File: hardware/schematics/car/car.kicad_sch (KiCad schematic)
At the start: 14 parts, among them M1 Motor_Servo, M2 Motor_DC, Q1 Q_PMOS_Depletion, SW1 RotaryEncoder, U1 VL53L0CXV0DH1, U2 VL53L0CXV0DH1, U3 VL53L0CXV0DH1, U5 TXS0108EPW, U6 TB6612FNG

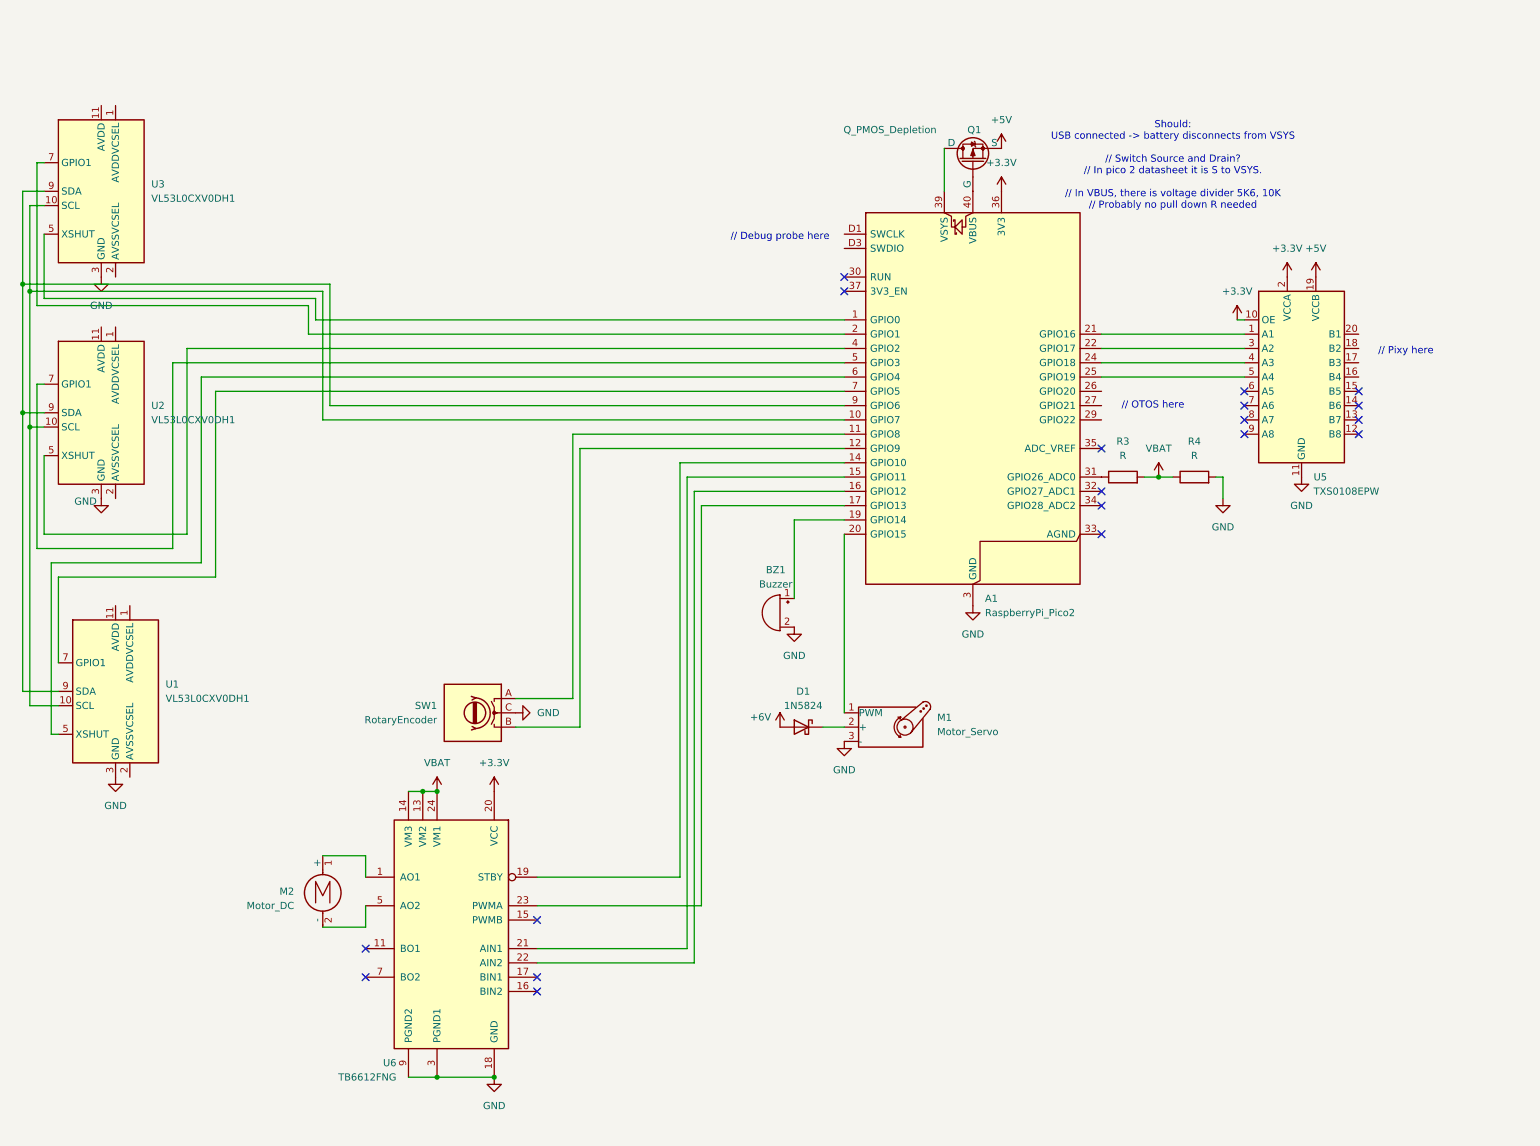
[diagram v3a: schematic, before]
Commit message: [Schematic] Add OTOS, Pixy, Debug probe, 2 buttons, fix voltage divider
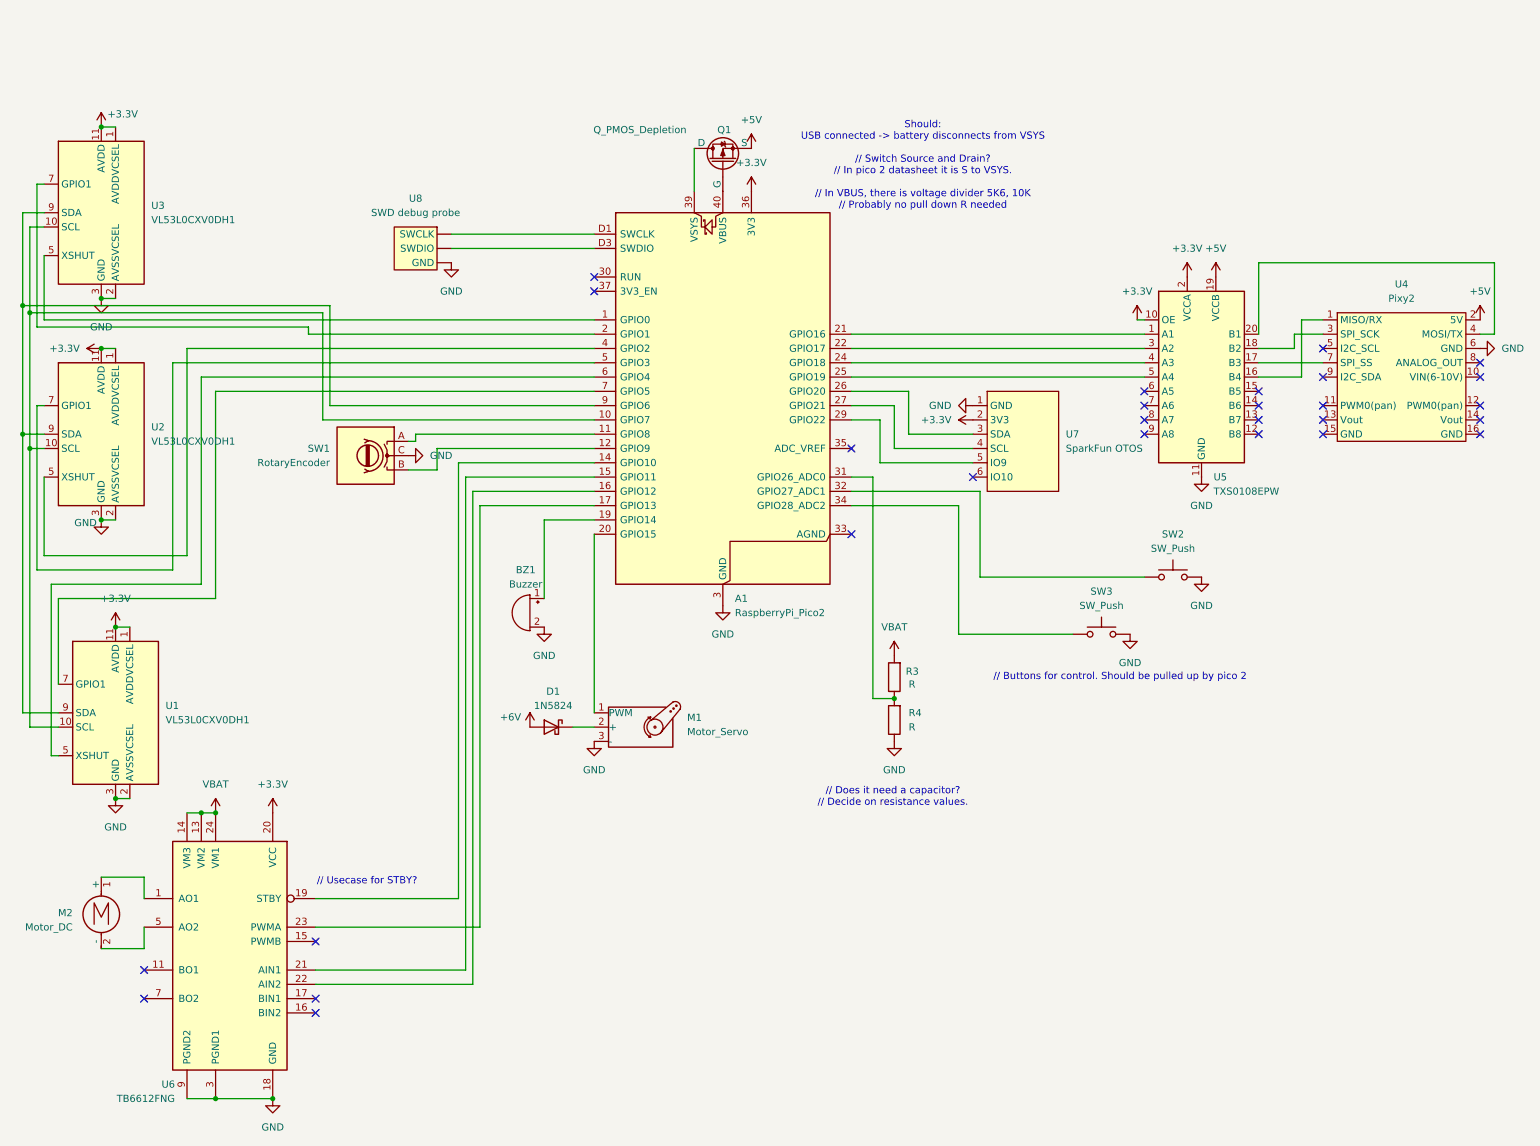
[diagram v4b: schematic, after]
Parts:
- added SW2, SW3: SW_Push, symbol Switch:SW_Push
- added U4: Pixy2, symbol xlnc_apex:Pixy2
- added U7: SparkFun OTOS, symbol xlnc_apex:SparkFun_OTOS
- added U8: SWD debug probe, symbol xlnc_apex:SWD_Debug_Probe
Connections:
- net +3.3V: now also U1.1 (AVDDVCSEL), U1.11 (AVDD), U2.1 (AVDDVCSEL), U2.11 (AVDD), U3.1 (AVDDVCSEL), U3.11 (AVDD), U7.2 (3V3)
- net +5V: now also U4.2 (5V)
- net GND: now also R4.1, U1.2 (AVSSVCSEL), U2.2 (AVSSVCSEL), U3.2 (AVSSVCSEL), SW2.2, SW3.2, U4.6 (GND), U7.1 (GND), U8. (GND); no longer R4.2
- net VBAT: no longer R4.1
- net at U5.16 (B4): now also U4.1 (MISO/RX)
- net at U5.17 (B3): now also U4.7 (SPI_SS)
- net at U5.18 (B2): now also U4.3 (SPI_SCK)
- net at U5.20 (B1): now also U4.4 (MOSI/TX)
- net at A1.31 (GPIO26_ADC0), R3.1: now also R4.2
- net at A1.26 (GPIO20): now also U7.3 (SDA)
- net at A1.27 (GPIO21): now also U7.4 (SCL)
- net at A1.29 (GPIO22): now also U7.5 (IO9)
- net at A1.32 (GPIO27_ADC1): now also SW2.1
- net at A1.34 (GPIO28_ADC2): now also SW3.1
- net at A1.D1 (SWCLK): now also U8. (GND)
- net at A1.D3 (SWDIO): now also U8. (GND)
- no-connect marks 19 -> 28
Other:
- note added: "// Buttons for control. Should be pulled up by pico 2"
- note added: "// Does it need a capacitor? // Decide on resistance values."
- note added: "// Usecase for STBY?"
- note removed: "// Debug probe here"
- note removed: "// OTOS here"
- note removed: "// Pixy here"
- moved on the sheet: A1, BZ1, D1, M1, M2, Q1, R3, R4, SW1, U1, U2, U3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

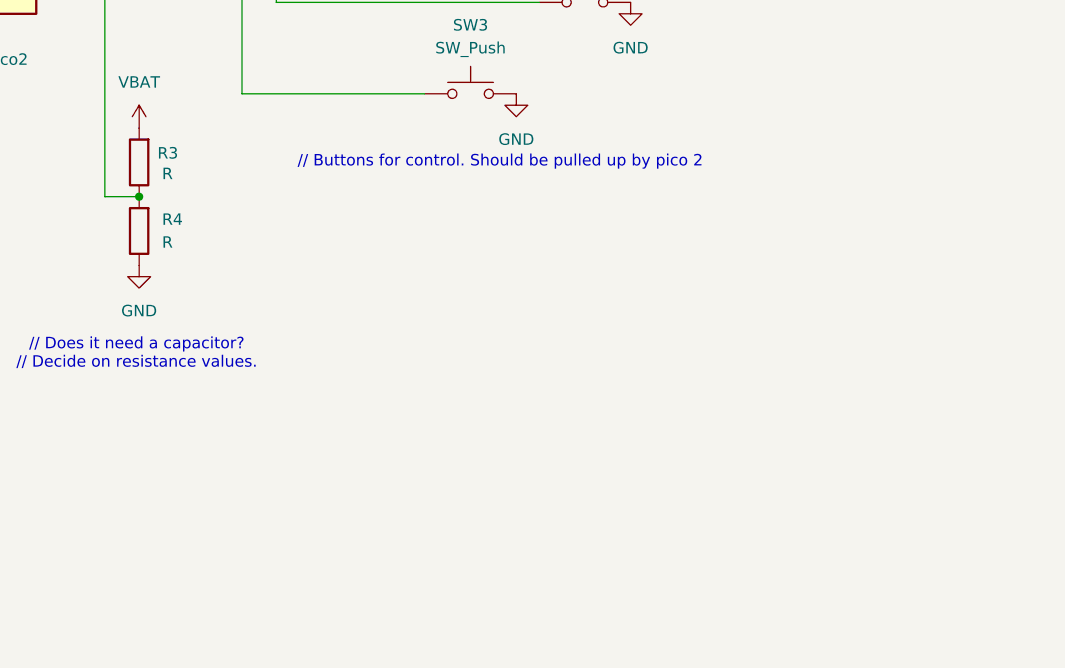
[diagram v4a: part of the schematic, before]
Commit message: [Schematic] Add buck converters, put resitances on ADC.
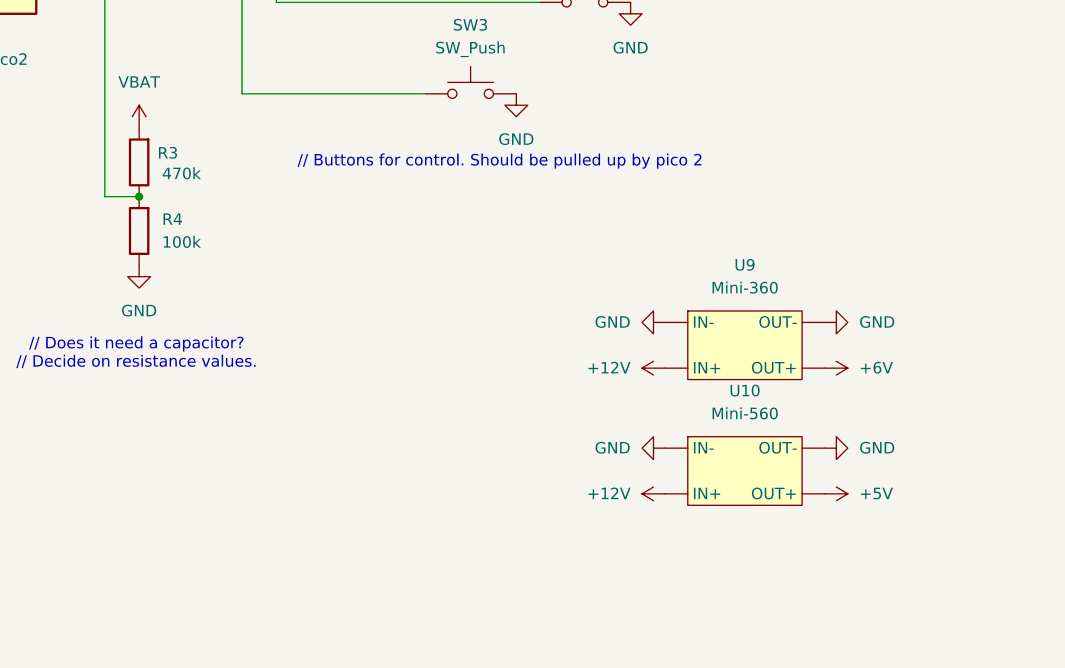
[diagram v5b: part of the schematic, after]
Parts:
- added U10: Mini-560, xlnc-foot:Buck_Mini-560, symbol xlnc_apex:mini560
- added U9: Mini-360, xlnc-foot:Buck_Mini-360, symbol xlnc_apex:mini360
- R3: value R -> 470k
- R4: value R -> 100k
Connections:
- net +5V: now also U10. (OUT+)
- net +6V: now also U9. (OUT+)
- net GND: now also U10. (OUT+), U9. (OUT+)
- new net +12V: U10. (OUT+), U9. (OUT+)

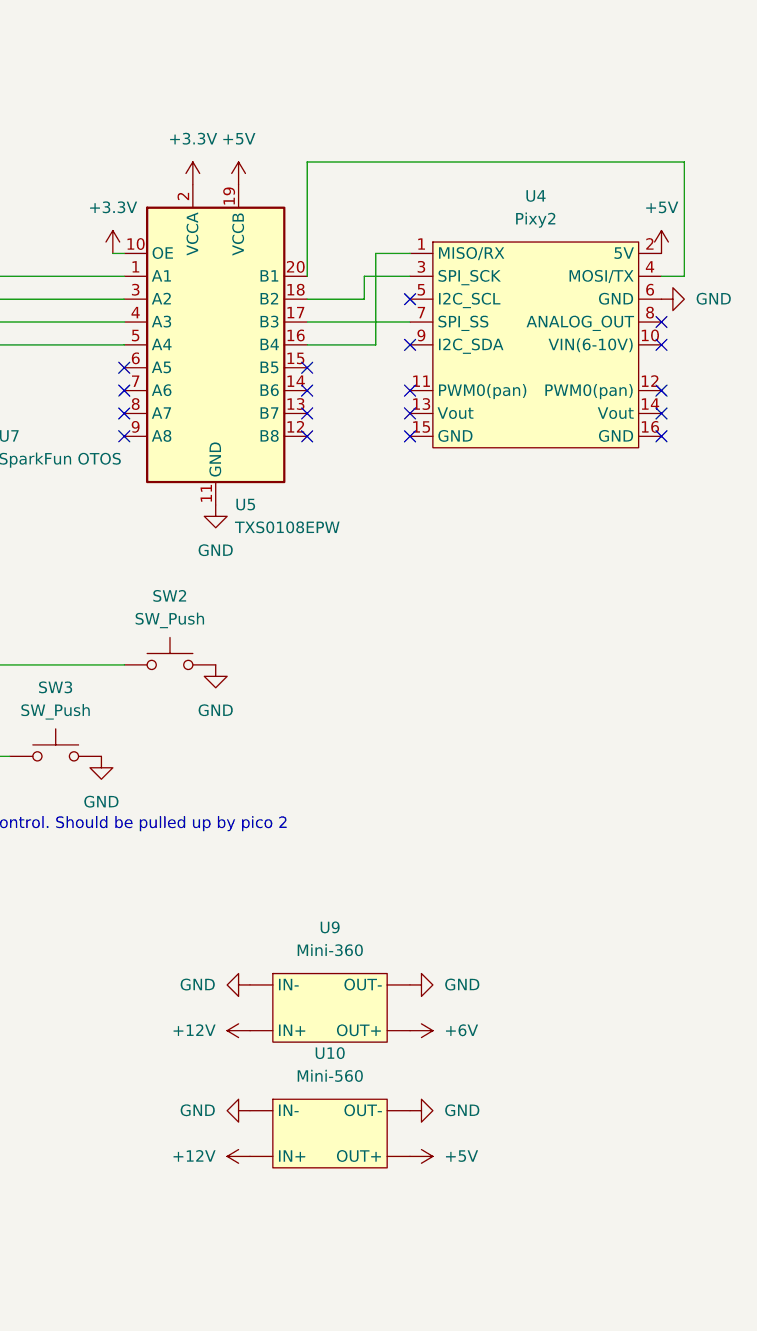
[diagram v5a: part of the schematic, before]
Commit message: [Schematic] Major work: add many perfboard footprints, fix spi wrong
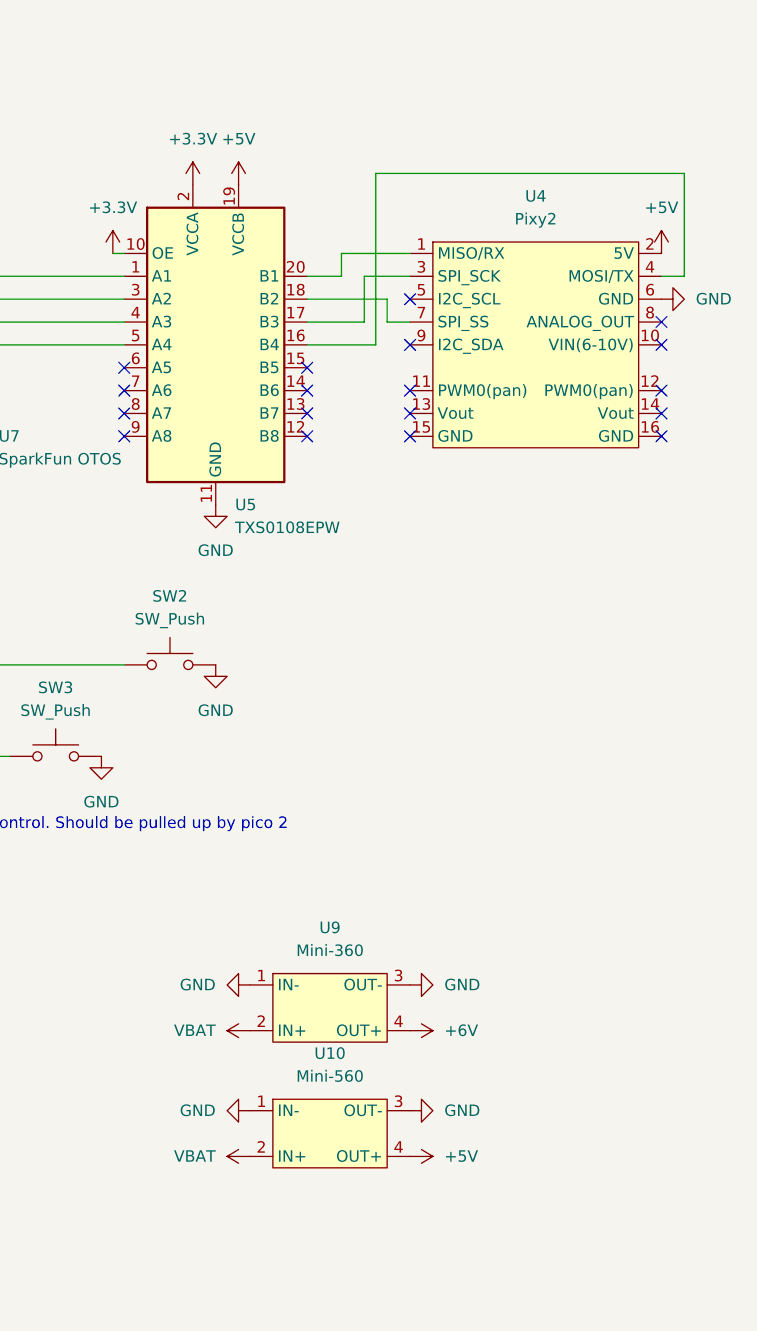
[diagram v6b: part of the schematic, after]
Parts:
- Q1: footprint (none) -> Connector_PinHeader_2.54mm:PinHeader_1x03_P2.54mm_Vertical
- R3, R4: footprint (none) -> Resistor_THT:R_Axial_DIN0204_L3.6mm_D1.6mm_P2.54mm_Vertical
- SW1, SW2, SW3: footprint (none) -> Connector_PinHeader_2.54mm:PinHeader_1x02_P2.54mm_Vertical
- U1, U2, U3: footprint Sensor_Distance:ST_VL53L1x -> xlnc-foot:VL53L0/1XV2_PinHeader_1x06_P2.54mm_Vertical
- U10: footprint xlnc-foot:Buck_Mini-560 -> xlnc-foot:Buck_Mini-560_2.54mm
- U4: footprint (none) -> xlnc-foot:Pixy2_PinHeader_1x06_P2.54mm_Vertical
- U7: footprint (none) -> Connector_PinHeader_2.54mm:PinHeader_1x05_P2.54mm_Vertical
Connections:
- net +5V: now also U10.4 (OUT+); no longer U10. (OUT+)
- net +6V: now also U9.4 (OUT+); no longer U9. (OUT+)
- net GND: now also U10.1 (IN-), U10.3 (OUT-), U9.1 (IN-), U9.3 (OUT-); no longer U10. (OUT+), U9. (OUT+)
- net VBAT: now also U10.2 (IN+), U9.2 (IN+)
- net at U5.16 (B4): now also U4.4 (MOSI/TX); no longer U4.1 (MISO/RX)
- net at U5.17 (B3): now also U4.3 (SPI_SCK); no longer U4.7 (SPI_SS)
- net at U5.18 (B2): now also U4.7 (SPI_SS); no longer U4.3 (SPI_SCK)
- net at U5.20 (B1): now also U4.1 (MISO/RX); no longer U4.4 (MOSI/TX)
- removed net +12V: U10. (OUT+), U9. (OUT+)
